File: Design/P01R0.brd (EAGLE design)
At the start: 28 x 26.7 mm, 27 parts, among them P2 PENTABIT_17.32, Q1 MMBT3904LT1, Q2 MMBT3904LT1, Q3 MMBT3904LT1, U1 STM32G0B1CEU6NUFQFPN48_STM32_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, X1 XTALL_CSTCE8M00G52

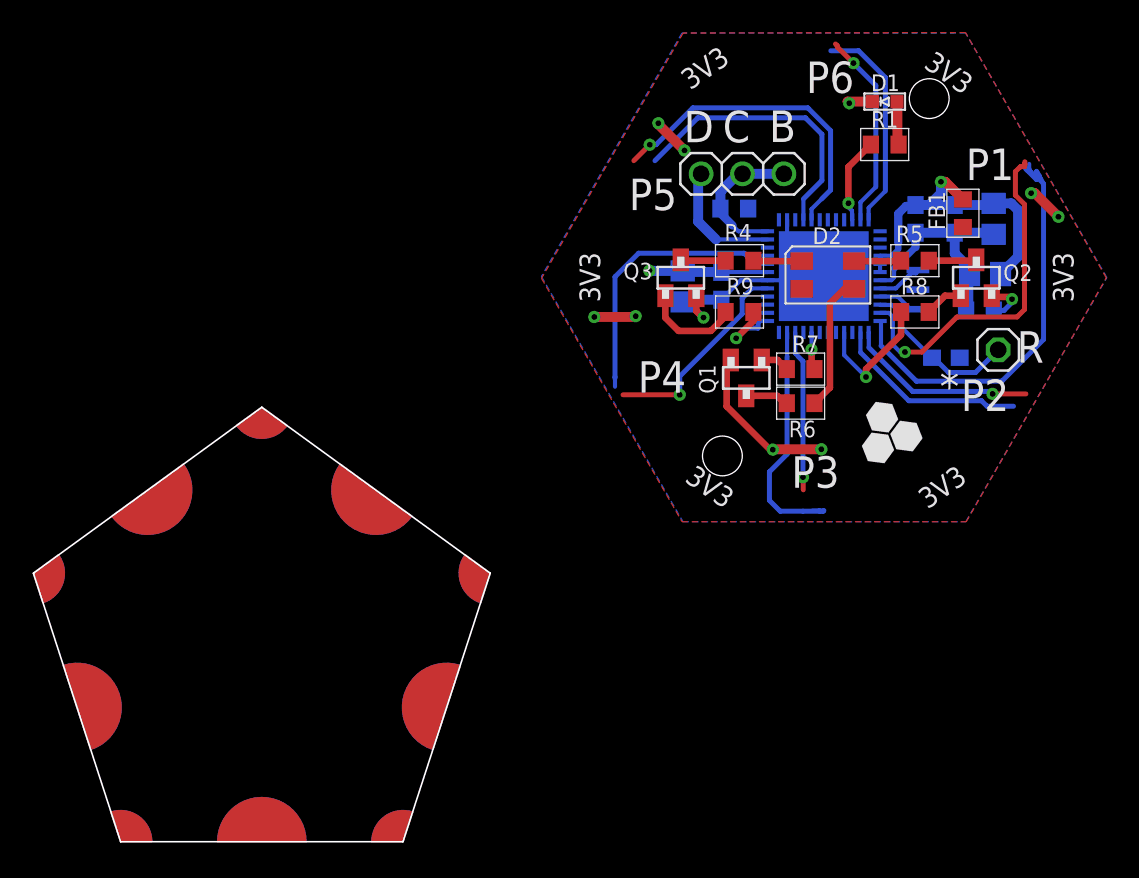
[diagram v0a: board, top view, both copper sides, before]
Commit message: -Changing the MCU to STM32G0B1CEU6N -Adding TVS 3.3V -Reviewed version , all finish
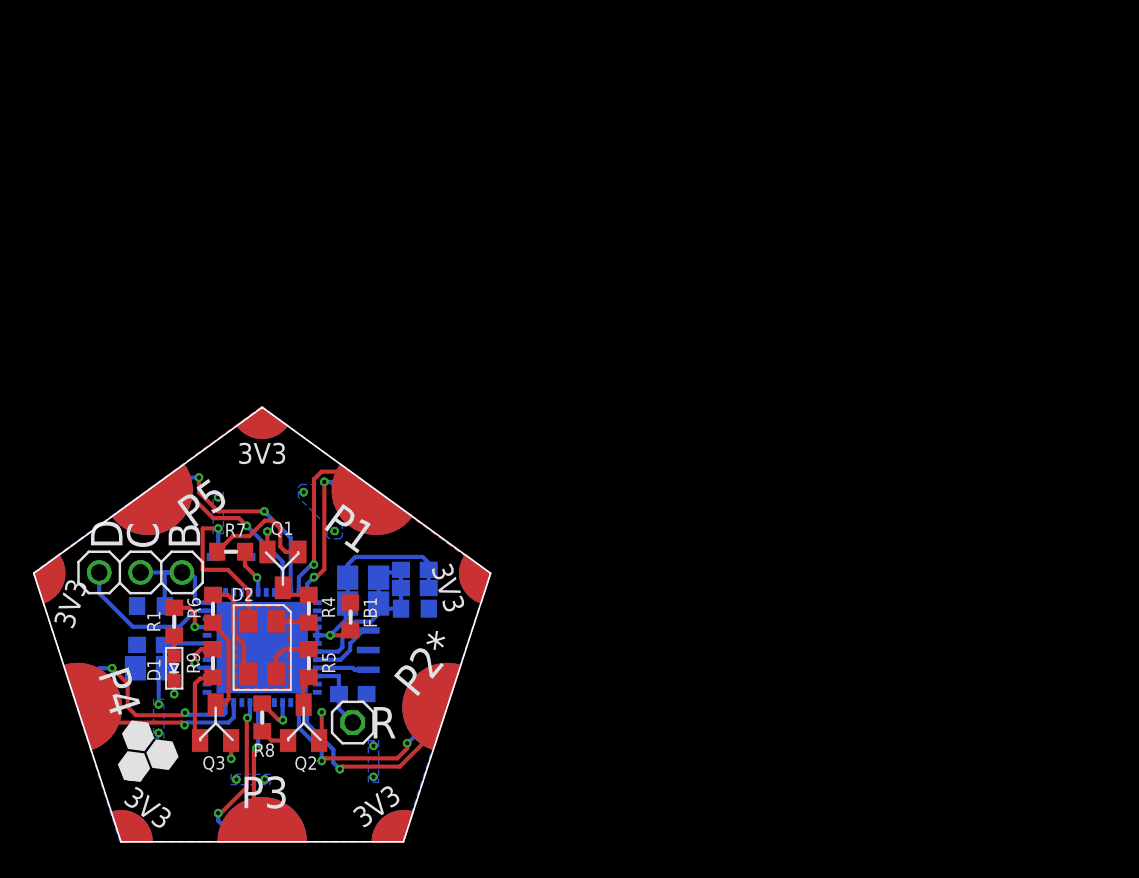
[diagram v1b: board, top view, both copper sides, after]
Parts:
- removed C8: 100nF, HEXABITZ_RCLS:C-0603
- removed JP1: R, HEXABITZ_USER_INTERFACE_PARTS:1X01
- removed JP2: (no value), pinhead:1X03
- removed P2: PENTABIT_17.32, hexabitz_connectors:PENTABIT_17.32
- added C1: 100nF, HEXABITZ_RCLS:C-0603
- added D3: BOURNS_CDSOD323-T03SCBOURNS_CDSOD323-T03SC_0_0, HEXABITZ_RCLS:BOURNS_CDSOD323-T03SC_0
- added P1: PENTABIT_17.32, hexabitz_connectors:PENTABIT_17.32
- added R: R, HEXABITZ_USER_INTERFACE_PARTS:1X01
- added SWD: (no value), HEXABITZ_CONNECTION_PARTS:1X03
- FB1: device HEXABITZ_RCLS:FB-TDK_MMZ1608Y300B -> HEXABITZ_RCLS:FB-0603
- U1: value STM32G0B1CEU6NUFQFPN48_STM32_STM -> STM32G0B1CEU6N; device HEXABITZ_ICs:UFQFPN48_STM32_STM -> HEXABITZ_ICs:HEXABITZ_ICS_QFN_B1CEU6_STM-L
- moved D1 55.7 mm to (-5.40, 10.6), turned to 0 degrees
- moved R1 52.5 mm to (-5.40, 13.5), turned to 270 degrees
- moved Q2 49.5 mm to (2.54, 7.30)
- moved R8 47.1 mm to (0.00, 7.62), turned to 270 degrees
- moved FB1 45.0 mm to (5.40, 13.8), turned to 90 degrees
- moved R5 44.6 mm to (2.86, 11.0), turned to 270 degrees
- moved C2 44.5 mm to (6.19, 16.2), turned to 180 degrees
- moved R3 43.3 mm to (-6.83, 14.4), turned to 180 degrees
- moved C7 43.2 mm to (6.19, 14.6), turned to 180 degrees
- moved D2 41.5 mm to (0.00, 11.9), turned to 270 degrees
- moved C3 41.3 mm to (-6.83, 12.1), turned to 0 degrees
- moved U1 41.3 mm to (0.00, 11.9)
- moved X1 40.3 mm to (6.51, 11.7)
- moved C4 40.2 mm to (-6.83, 10.6), turned to 0 degrees
- moved C6 39.5 mm to (9.37, 16.7), turned to 0 degrees
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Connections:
- net N$1 renamed KA_R
- net N$11 renamed Q2C
- net N$2 renamed KA_G
- net N$5 renamed OSC_OUT
- net N$6 renamed OSC_IN
- net N$8 renamed KA_B
- removed net CLK: JP2.1, JP2.2, R3.2, U1.36
- removed net DATA: JP2.3, U1.35
- removed net N$10: Q1.3, R6.2
- removed net N$12: Q3.3, R4.2
- removed net N$4: C8.1, JP1.1, U1.10
- removed net N$7: R1.1, U1.46
- new net LED_INDICATOR: R1.1, U1.33
- new net Q1C: Q1.3, R4.2
- new net Q3C: Q3.3, R6.2
- new net R: C1.1, R.1, U1.10
- new net SWCLK: R3.2, SWD.1, SWD.2, U1.36
- new net SWDIO: SWD.3, U1.35
- net BLED: now also R9.1, U1.28; no longer R7.1, U1.20
- net GND: now also C1.2, D3.1, P1.PAD_PD10, P1.PAD_PD6, P1.PAD_PD7, P1.PAD_PD8, P1.PAD_PD9; no longer C8.2, P2.PAD_PD10, P2.PAD_PD6, P2.PAD_PD7, P2.PAD_PD8, P2.PAD_PD9, U1.1, U1.2, U1.37, U1.38
- net RLED: now also R7.1, U1.42; no longer R9.1, U1.25
- net USART1_RX: now also P1.PAD_PD5, U1.46; no longer P2.PAD_PD4, U1.32
- net USART1_TX: now also P1.PAD_PU5, U1.45; no longer P2.PAD_PU4, U1.29
- net USART2_RX: now also P1.PAD_PD2; no longer P2.PAD_PD2
- net USART2_TX: now also P1.PAD_PU2; no longer P2.PAD_PU2
- net USART3_RX: now also P1.PAD_PD4; no longer P2.PAD_PD3
- net USART3_TX: now also P1.PAD_PU4; no longer P2.PAD_PU3
- net USART4_RX: no longer P2.PAD_PD1
- net USART4_TX: no longer P2.PAD_PU1
- net USART5_RX: now also P1.PAD_PD3, U1.20; no longer P2.PAD_PD5, U1.40
- net USART5_TX: now also P1.PAD_PU3, U1.19; no longer P2.PAD_PU5, U1.41
- net USART6_RX: now also P1.PAD_PD1
- net USART6_TX: now also P1.PAD_PU1
- net VDD: now also D3.2, P1.PAD_PU10, P1.PAD_PU6, P1.PAD_PU7, P1.PAD_PU8, P1.PAD_PU9; no longer P2.PAD_PU10, P2.PAD_PU6, P2.PAD_PU7, P2.PAD_PU8, P2.PAD_PU9
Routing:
- net GND: track 32.6 -> 5.02 mm, vias 11 -> 4
- net USART4_RX: track 27.5 -> 0.00 mm
- net USART4_TX: track 21.7 -> 0.00 mm, vias 1 -> 0
- net USART5_TX: track 19.9 -> 8.31 mm
- net N$4: track 10.3 -> 0.00 mm
- net VDD: track 7.27 -> 17.1 mm, vias 1 -> 10
- net CLK: track 9.42 -> 0.00 mm
- net SWDIO: track 0.00 -> 9.15 mm
- net SWCLK: track 0.00 -> 8.71 mm
- net DATA: track 7.71 -> 0.00 mm
- net VDDA: track 21.0 -> 14.9 mm
- net USART5_RX: track 17.5 -> 11.4 mm, vias 0 -> 2
- net Q3C: track 0.00 -> 6.03 mm
- net GLED: track 8.18 -> 2.77 mm
- net N$7: track 5.35 -> 0.00 mm, vias 1 -> 0
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- added copper zone on layer 16, net VDD
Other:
- board size 28 x 26.7 mm -> 28 x 26.6 mm
- board text added: "P2*"
- board text removed: "*"
- board text removed: "."
- board text removed: "P2"
- board text removed: "P6"

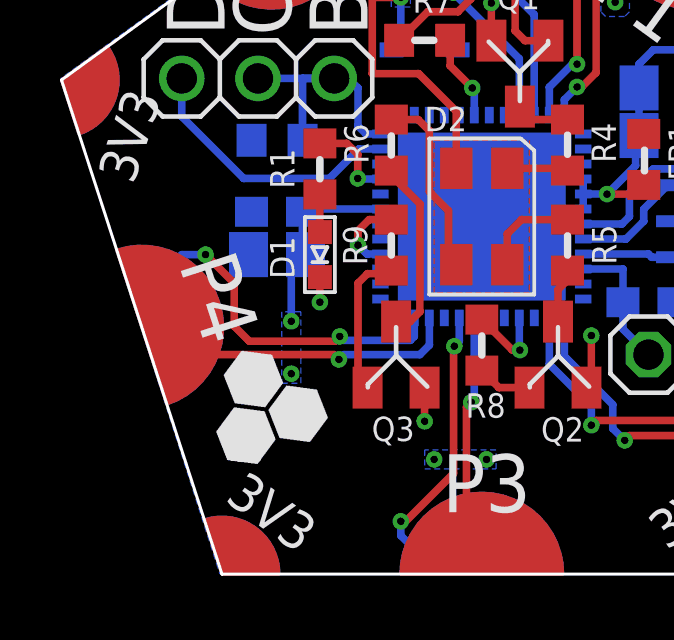
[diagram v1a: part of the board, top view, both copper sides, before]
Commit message: Update the Logo
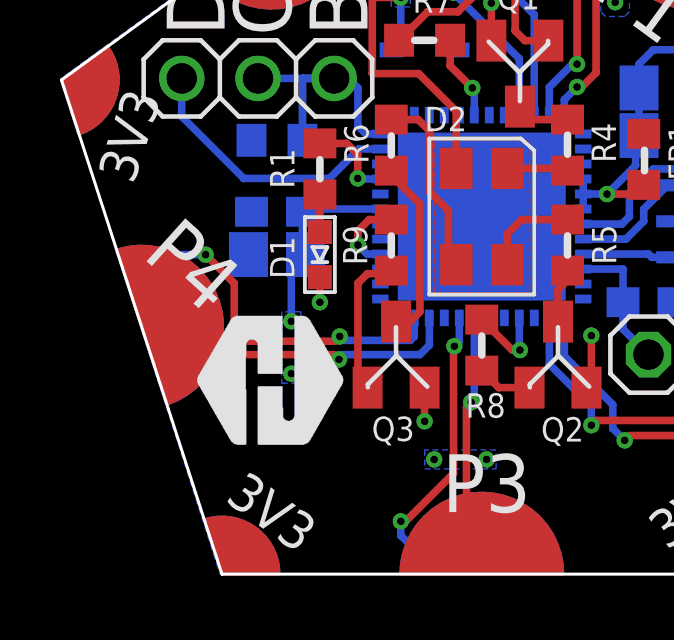
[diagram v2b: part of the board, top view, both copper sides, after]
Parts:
- added TRIMBLE-LOGO1: HEXA-LOGO, HEXABITZ_USER_INTERFACE_PARTS:HEXA-LOGO

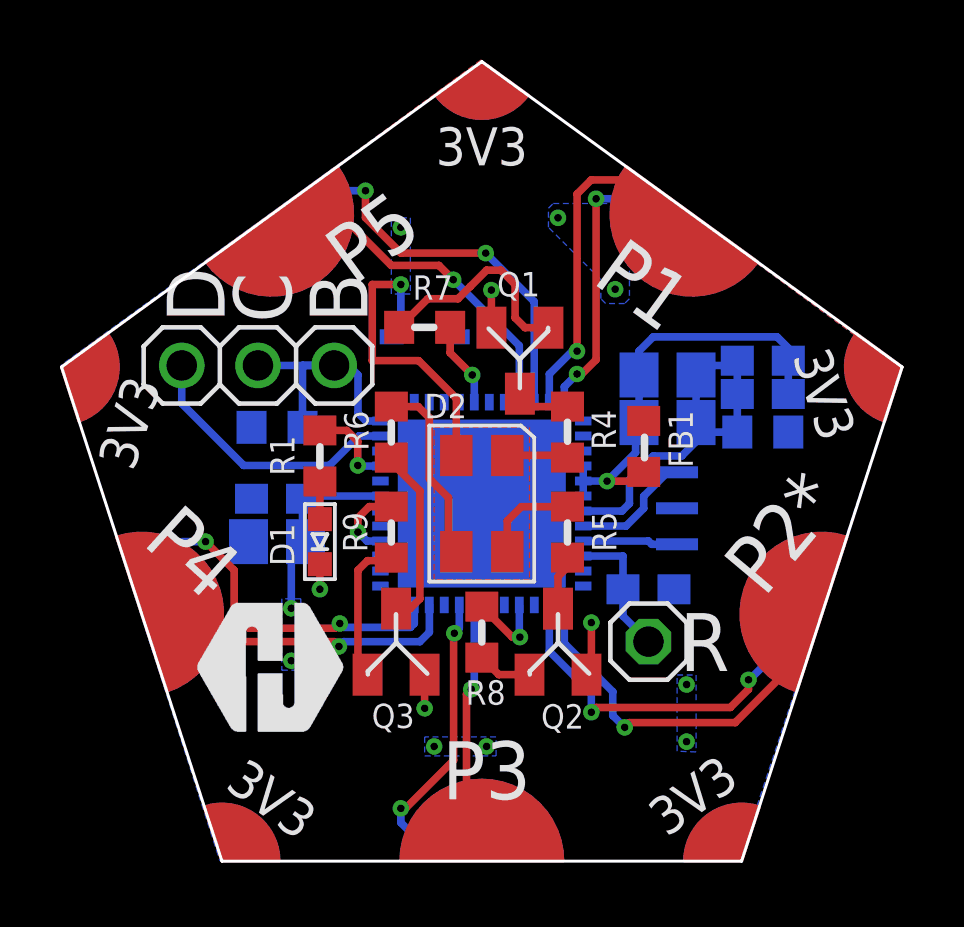
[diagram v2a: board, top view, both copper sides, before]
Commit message: -Add TVS diode -Change the MCU to STM32G0B1CEU6 -Activate the thermal option for the polygon -Improve the layout design for better appearence
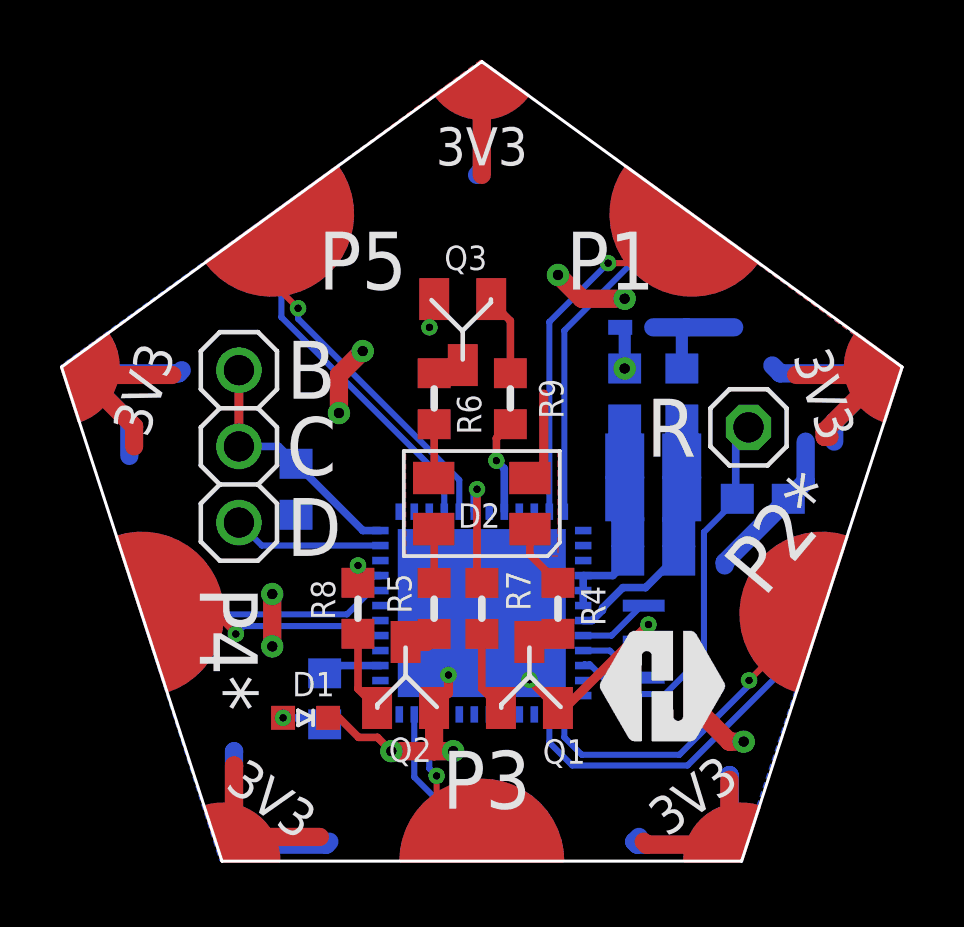
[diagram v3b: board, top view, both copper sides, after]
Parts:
- removed C3: 100nF, HEXABITZ_RCLS:C-0603
- removed C4: 4.7uF, HEXABITZ_RCLS:C-0805-POL
- C2, C7: device HEXABITZ_RCLS:C-0805-POL -> HEXABITZ_RCLS:C-0805
- D1: value VLMS1300-GS08 -> RED
- U1: value STM32G0B1CEU6N -> STM32G0B1CEU6QFN_B1CEU6_STM-L; device HEXABITZ_ICs:HEXABITZ_ICS_QFN_B1CEU6_STM-L -> HEXABITZ_ICs:QFN_B1CEU6_STM-L
- moved TRIMBLE-LOGO1 13.0 mm to (6.03, 3.97)
- moved Q3 10.6 mm to (-0.64, 17.6), turned to 180 degrees
- moved Q1 10.5 mm to (1.59, 6.19), turned to 0 degrees
- moved R7 9.56 mm to (0.00, 8.41), turned to 270 degrees
- moved R1 8.10 mm to (-5.24, 5.40), flipped to the bottom
- moved R 7.88 mm to (8.89, 14.4)
- moved D3 7.63 mm to (5.71, 17.8)
- moved C6 7.60 mm to (5.71, 10.0), turned to 180 degrees
- moved R9 5.96 mm to (0.95, 15.4), turned to 90 degrees
- moved D1 5.89 mm to (-5.87, 4.76), turned to 90 degrees
- moved R4 5.88 mm to (2.54, 8.41), turned to 270 degrees
- moved C5 5.88 mm to (5.71, 11.0), turned to 180 degrees
- moved Q2 5.20 mm to (-2.54, 6.19)
- moved R5 5.12 mm to (-1.59, 8.41)
- moved C1 4.86 mm to (9.37, 12.1)
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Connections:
- removed net USART4_RX: U1.12
- removed net USART4_TX: U1.11
- net BLED: now also U1.44; no longer U1.28
- net GLED: now also U1.33; no longer U1.16
- net GND: no longer C3.2, C4.2, U1.30
- net LED_INDICATOR: now also U1.27; no longer U1.33
- net USART1_RX: now also P1.PAD_PD4, U1.32; no longer P1.PAD_PD5, U1.46
- net USART1_TX: now also P1.PAD_PU4, U1.29; no longer P1.PAD_PU5, U1.45
- net USART3_RX: now also P1.PAD_PD3; no longer P1.PAD_PD4
- net USART3_TX: now also P1.PAD_PU3; no longer P1.PAD_PU4
- net USART5_RX: now also P1.PAD_PD5, U1.40; no longer P1.PAD_PD3, U1.20
- net USART5_TX: now also P1.PAD_PU5, U1.41; no longer P1.PAD_PU3, U1.19
- net VDD: no longer C3.1, C4.1, U1.31
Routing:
- net GND: track 5.02 -> 66.9 mm, vias 4 -> 14
- net VDD: track 17.1 -> 30.4 mm, vias 10 -> 1
- net R: track 4.53 -> 13.3 mm
- net USART3_RX: track 13.1 -> 5.27 mm, vias 2 -> 0
- net VDDA: track 14.9 -> 7.44 mm, vias 1 -> 0
- net USART1_RX: track 14.4 -> 7.84 mm, vias 2 -> 0
- net USART3_TX: track 11.0 -> 5.06 mm
- net Q3C: track 6.03 -> 1.07 mm
- net N$15: track 7.21 -> 2.74 mm
- net KA_B: track 6.26 -> 1.80 mm
- net VSSA: track 13.0 -> 8.80 mm
- net SWDIO: track 9.15 -> 5.03 mm
- net USART5_TX: track 8.31 -> 11.9 mm
- net USART1_TX: track 11.4 -> 8.02 mm
- net N$13: track 4.90 -> 2.74 mm
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- removed copper zone on layer 16, net VDD
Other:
- board text added: "P4*"
- board text removed: "P4"
